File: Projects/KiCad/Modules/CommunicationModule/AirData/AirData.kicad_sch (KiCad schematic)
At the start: 30 parts, among them J1 Conn_01x08, SW1 SW_DIP_x02, U1 MCP2562-E-P, U2 MCP2515-I/P, U3 NJM7805SDL1, U4 ABX00012, Y1 8MHz

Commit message: チップ積層セラミックコンデンサをSMD1608に変更
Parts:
- C2: value 0.33μF -> 10μF; footprint Capacitor_SMD:C_0805_2012Metric_Pad1.18x1.45mm_HandSolder -> Capacitor_SMD:C_0603_1608Metric_Pad1.08x0.95mm_HandSolder
- C3, C4, C5, C6: footprint Capacitor_SMD:C_0805_2012Metric_Pad1.18x1.45mm_HandSolder -> Capacitor_SMD:C_0603_1608Metric_Pad1.08x0.95mm_HandSolder
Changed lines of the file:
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@@
       (effects (font (size 1.27 1.27)) (justify left))
     )
-    (property "Footprint" "Capacitor_SMD:C_0805_2012Metric_Pad1.18x1.45mm_HandSolder" (at 97.4852 35.56 0)
+    (property "Footprint" "Capacitor_SMD:C_0603_1608Metric_Pad1.08x0.95mm_HandSolder" (at 97.4852 35.56 0)
       (effects (font (size 1.27 1.27)) hide)
     )
@@
       (effects (font (size 1.27 1.27)) (justify left))
     )
-    (property "Footprint" "Capacitor_SMD:C_0805_2012Metric_Pad1.18x1.45mm_HandSolder" (at 150.8252 30.48 0)
+    (property "Footprint" "Capacitor_SMD:C_0603_1608Metric_Pad1.08x0.95mm_HandSolder" (at 150.8252 30.48 0)
       (effects (font (size 1.27 1.27)) hide)
     )
@@
       (effects (font (size 1.27 1.27)) (justify left))
     )
-    (property "Footprint" "Capacitor_SMD:C_0805_2012Metric_Pad1.18x1.45mm_HandSolder" (at 88.5952 35.56 0)
+    (property "Footprint" "Capacitor_SMD:C_0603_1608Metric_Pad1.08x0.95mm_HandSolder" (at 88.5952 35.56 0)
       (effects (font (size 1.27 1.27)) hide)
     )
@@
       (effects (font (size 1.27 1.27)) (justify left))
     )
-    (property "Footprint" "Capacitor_SMD:C_0805_2012Metric_Pad1.18x1.45mm_HandSolder" (at 223.2152 113.03 0)
+    (property "Footprint" "Capacitor_SMD:C_0603_1608Metric_Pad1.08x0.95mm_HandSolder" (at 223.2152 113.03 0)
       (effects (font (size 1.27 1.27)) hide)
     )
@@
       (effects (font (size 1.27 1.27)) (justify left))
     )
-    (property "Value" "0.33μF" (at 200.66 111.125 0)
-      (effects (font (size 1.27 1.27)) (justify left))
-    )
-    (property "Footprint" "Capacitor_SMD:C_0805_2012Metric_Pad1.18x1.45mm_HandSolder" (at 197.8152 113.03 0)
-      (effects (font (size 1.27 1.27)) hide)
-    )
+    (property "Value" "10μF" (at 200.66 111.125 0)
+      (effects (font (size 1.27 1.27)) (justify left))
+    )
+    (property "Footprint" "Capacitor_SMD:C_0603_1608Metric_Pad1.08x0.95mm_HandSolder" (at 197.8152 113.03 0)
+      (effects (font (size 1.27 1.27)) hide)
+    )

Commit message: 抵抗の在庫に合わせてサイズを変更
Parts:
- R3, R4, R5, R6, R7: footprint Resistor_SMD:R_0603_1608Metric_Pad0.98x0.95mm_HandSolder -> Resistor_SMD:R_0805_2012Metric_Pad1.20x1.40mm_HandSolder
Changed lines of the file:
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@@
       (effects (font (size 1.27 1.27)))
     )
-    (property "Footprint" "Resistor_SMD:R_0603_1608Metric_Pad0.98x0.95mm_HandSolder" (at 156.21 70.358 90)
+    (property "Footprint" "Resistor_SMD:R_0805_2012Metric_Pad1.20x1.40mm_HandSolder" (at 156.21 70.358 90)
       (effects (font (size 1.27 1.27)) hide)
     )
@@
       (effects (font (size 1.27 1.27)) (justify left))
     )
-    (property "Footprint" "Resistor_SMD:R_0603_1608Metric_Pad0.98x0.95mm_HandSolder" (at 61.722 166.37 90)
+    (property "Footprint" "Resistor_SMD:R_0805_2012Metric_Pad1.20x1.40mm_HandSolder" (at 61.722 166.37 90)
       (effects (font (size 1.27 1.27)) hide)
     )
@@
       (effects (font (size 1.27 1.27)) (justify left))
     )
-    (property "Footprint" "Resistor_SMD:R_0603_1608Metric_Pad0.98x0.95mm_HandSolder" (at 82.042 166.37 90)
+    (property "Footprint" "Resistor_SMD:R_0805_2012Metric_Pad1.20x1.40mm_HandSolder" (at 82.042 166.37 90)
       (effects (font (size 1.27 1.27)) hide)
     )
@@
       (effects (font (size 1.27 1.27)) (justify left))
     )
-    (property "Footprint" "Resistor_SMD:R_0603_1608Metric_Pad0.98x0.95mm_HandSolder" (at 71.882 166.37 90)
+    (property "Footprint" "Resistor_SMD:R_0805_2012Metric_Pad1.20x1.40mm_HandSolder" (at 71.882 166.37 90)
       (effects (font (size 1.27 1.27)) hide)
     )
@@
       (effects (font (size 1.27 1.27)) (justify left))
     )
-    (property "Footprint" "Resistor_SMD:R_0603_1608Metric_Pad0.98x0.95mm_HandSolder" (at 92.202 166.37 90)
-      (effects (font (size 1.27 1.27)) hide)
-    )
+    (property "Footprint" "Resistor_SMD:R_0805_2012Metric_Pad1.20x1.40mm_HandSolder" (at 92.202 166.37 90)
+      (effects (font (size 1.27 1.27)) hide)
+    )

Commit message: コネクタのピン配置を変更
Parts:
- J1: footprint Connector_Hirose:Hirose_DF11-8DP-2DSA_2x04_P2.00mm_Vertical -> Hirose_Connector:Hirose_DF11B-8DP-2DS
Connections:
- net CAN_L: now also J1.5 (Pin_5), J1.6 (Pin_6); no longer J1.3 (Pin_3), J1.4 (Pin_4)
- net GND: now also J1.3 (Pin_3), J1.4 (Pin_4); no longer J1.5 (Pin_5), J1.6 (Pin_6)
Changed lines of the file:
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@@
     (stroke (width 0) (type default))
-  )
-  (label "CAN_L" (at 43.18 35.56 180) (fields_autoplaced)
-    (effects (font (size 1.27 1.27)) (justify right bottom))
   )
   (label "CAN_H" (at 43.18 25.4 180) (fields_autoplaced)
@@
     (effects (font (size 1.27 1.27)) (justify left bottom))
   )
-  (label "GND" (at 43.18 30.48 180) (fields_autoplaced)
-    (effects (font (size 1.27 1.27)) (justify right bottom))
-  )
   (label "CAN_H" (at 43.18 53.34 180) (fields_autoplaced)
     (effects (font (size 1.27 1.27)) (justify right bottom))
@@
   )
   (label "+12V" (at 43.18 40.64 180) (fields_autoplaced)
+    (effects (font (size 1.27 1.27)) (justify right bottom))
+  )
+  (label "GND" (at 43.18 35.56 180) (fields_autoplaced)
+    (effects (font (size 1.27 1.27)) (justify right bottom))
+  )
+  (label "CAN_L" (at 43.18 30.48 180) (fields_autoplaced)
     (effects (font (size 1.27 1.27)) (justify right bottom))
   )
@@
       (effects (font (size 1.27 1.27)))
     )
-    (property "Footprint" "Connector_Hirose:Hirose_DF11-8DP-2DSA_2x04_P2.00mm_Vertical" (at 26.67 34.29 0)
-      (effects (font (size 1.27 1.27)) hide)
-    )
+    (property "Footprint" "Hirose_Connector:Hirose_DF11B-8DP-2DS" (at 26.67 34.29 0)
+      (effects (font (size 1.27 1.27)) hide)
+    )

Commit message: クリスタルをSMDに変更
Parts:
- Y1: footprint Crystal:Crystal_HC49-U_Vertical -> Crystal:Crystal_SMD_HC49-SD
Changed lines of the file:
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@@
       (effects (font (size 1.27 1.27)) (justify right))
     )
-    (property "Footprint" "Crystal:Crystal_HC49-U_Vertical" (at 257.81 33.02 0)
+    (property "Footprint" "Crystal:Crystal_SMD_HC49-SD" (at 257.81 33.02 0)
       (effects (font (size 1.27 1.27)) hide)
     )

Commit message: バッファコンデンサを表面実装に変更
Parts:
- C8: value 100μF -> 47μF; footprint Capacitor_SMD:CP_Elec_6.3x7.7 -> Capacitor_SMD:CP_Elec_6.3x5.9
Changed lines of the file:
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@@
       (effects (font (size 1.27 1.27)) (justify left))
     )
-    (property "Value" "100μF" (at 238.76 110.236 0)
+    (property "Value" "47μF" (at 238.76 110.236 0)
       (effects (font (size 1.27 1.27)) (justify left))
     )
-    (property "Footprint" "Capacitor_SMD:CP_Elec_6.3x7.7" (at 235.9152 113.03 0)
+    (property "Footprint" "Capacitor_SMD:CP_Elec_6.3x5.9" (at 235.9152 113.03 0)
       (effects (font (size 1.27 1.27)) hide)
     )

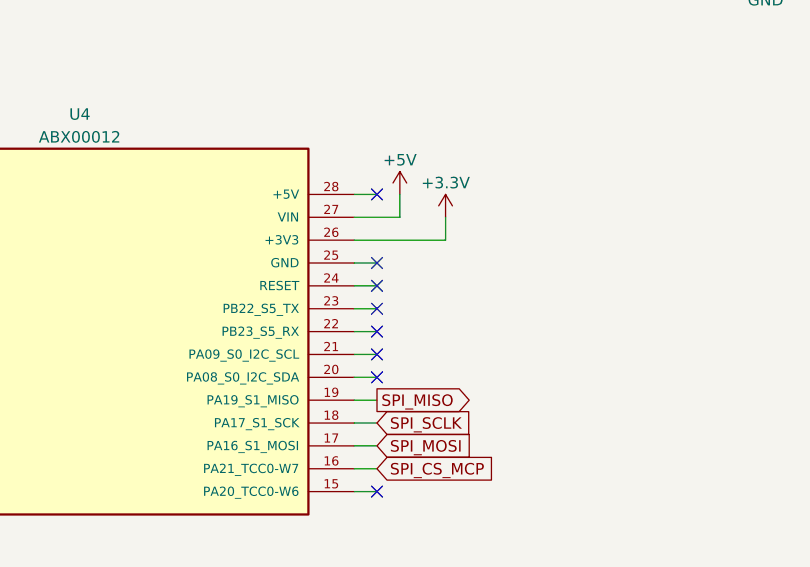
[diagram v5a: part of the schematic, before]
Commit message: 配線の繋ぎ忘れを修正
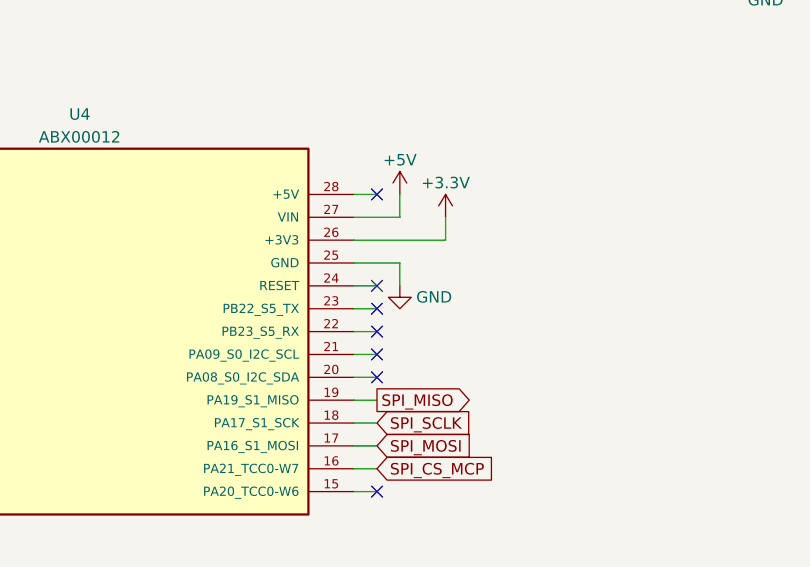
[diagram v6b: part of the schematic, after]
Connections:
- net GND: now also U4.25 (GND)
- no-connect marks 17 -> 16
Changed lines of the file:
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@@
   (no_connect (at 123.19 95.25))
   (no_connect (at 57.15 105.41))
-  (no_connect (at 123.19 102.87))
   (no_connect (at 57.15 110.49))
   (no_connect (at 57.15 95.25))
@@
     (stroke (width 0) (type default))
   )
-  (wire (pts (xy 120.65 102.87) (xy 123.19 102.87))
+  (wire (pts (xy 120.65 102.87) (xy 125.73 102.87))
     (stroke (width 0) (type default))
   )
@@
   )
   (wire (pts (xy 80.01 57.15) (xy 83.82 57.15))
+    (stroke (width 0) (type default))
+  )
+  (wire (pts (xy 125.73 102.87) (xy 125.73 105.41))
     (stroke (width 0) (type default))
   )
@@
         )
       )
+    )
+  )
+  (symbol (lib_id "power:GND") (at 125.73 105.41 0) (mirror y) (unit 1)
+    (in_bom yes) (on_board yes) (dnp no)
+    (property "Reference" "#PWR029" (at 125.73 111.76 0)
+      (effects (font (size 1.27 1.27)) hide)
+    )
+    (property "Value" "GND" (at 129.54 106.68 0)
+      (effects (font (size 1.27 1.27)))
+    )
+    (property "Footprint" "" (at 125.73 105.41 0)
+      (effects (font (size 1.27 1.27)) hide)
+    )
+    (property "Datasheet" "" (at 125.73 105.41 0)
+      (effects (font (size 1.27 1.27)) hide)
+    )
+    (pin "1")
+    (instances
+      (project "AirData"
+        (path "/ea1ed597-7cd3-4340-902e-bdce8f2d7a62"
+          (reference "#PWR029") (unit 1)
+        )
+      )

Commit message: ガーバーを再生成
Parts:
- C2: value 10μF -> 10uF
- C3, C4, C5, C6: value 0.1μF -> 0.1uF
- C8: value 47μF -> 47uF
- D2, D3, D5, D6: value ORANGE -> BLUE
- R1: value 120Ω -> 120R
- R2: value 620Ω -> 620R
- R3: value 10kΩ -> 10kR
- R4, R5, R6, R7: value 100Ω -> 100R
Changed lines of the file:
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@@
       (effects (font (size 1.27 1.27)) (justify right))
     )
-    (property "Value" "ORANGE" (at 97.79 179.3874 90)
+    (property "Value" "BLUE" (at 97.79 179.3874 90)
       (effects (font (size 1.27 1.27)) (justify right))
     )
@@
       (effects (font (size 1.27 1.27)) (justify right))
     )
-    (property "Value" "ORANGE" (at 67.31 179.3874 90)
+    (property "Value" "BLUE" (at 67.31 179.3874 90)
       (effects (font (size 1.27 1.27)) (justify right))
     )
@@
       (effects (font (size 1.27 1.27)))
     )
-    (property "Value" "10kΩ" (at 156.21 66.04 90)
+    (property "Value" "10kR" (at 156.21 66.04 90)
       (effects (font (size 1.27 1.27)))
     )
@@
       (effects (font (size 1.27 1.27)) (justify left))
     )
-    (property "Value" "0.1μF" (at 99.06 33.02 0)
+    (property "Value" "0.1uF" (at 99.06 33.02 0)
       (effects (font (size 1.27 1.27)) (justify left))
     )
@@
       (effects (font (size 1.27 1.27)) (justify left))
     )
-    (property "Value" "47μF" (at 238.76 110.236 0)
+    (property "Value" "47uF" (at 238.76 110.236 0)
       (effects (font (size 1.27 1.27)) (justify left))
     )
@@
       (effects (font (size 1.27 1.27)) (justify right))
     )
-    (property "Value" "ORANGE" (at 87.63 179.3874 90)
+    (property "Value" "BLUE" (at 87.63 179.3874 90)
       (effects (font (size 1.27 1.27)) (justify right))
     )
@@
       (effects (font (size 1.27 1.27)) (justify left))
     )
-    (property "Value" "100Ω" (at 66.04 167.6399 0)
+    (property "Value" "100R" (at 66.04 167.6399 0)
       (effects (font (size 1.27 1.27)) (justify left))
     )
@@
       (effects (font (size 1.27 1.27)) (justify left))
     )
-    (property "Value" "0.1μF" (at 152.4 27.94 0)
+    (property "Value" "0.1uF" (at 152.4 27.94 0)
       (effects (font (size 1.27 1.27)) (justify left))
     )
@@
       (effects (font (size 1.27 1.27)) (justify left))
     )
-    (property "Value" "100Ω" (at 86.36 167.6399 0)
+    (property "Value" "100R" (at 86.36 167.6399 0)
       (effects (font (size 1.27 1.27)) (justify left))
     )
@@
       (effects (font (size 1.27 1.27)) (justify left))
     )
-    (property "Value" "0.1μF" (at 90.17 33.02 0)
+    (property "Value" "0.1uF" (at 90.17 33.02 0)
       (effects (font (size 1.27 1.27)) (justify left))
     )
@@
       (effects (font (size 1.27 1.27)) (justify left))
     )
-    (property "Value" "0.1μF" (at 226.06 111.125 0)
+    (property "Value" "0.1uF" (at 226.06 111.125 0)
       (effects (font (size 1.27 1.27)) (justify left))
     )
@@
       (effects (font (size 1.27 1.27)) (justify left))
     )
-    (property "Value" "10μF" (at 200.66 111.125 0)
+    (property "Value" "10uF" (at 200.66 111.125 0)
       (effects (font (size 1.27 1.27)) (justify left))
     )
@@
       (effects (font (size 1.27 1.27)) (justify left))
     )
-    (property "Value" "620Ω" (at 57.15 167.6399 0)
+    (property "Value" "620R" (at 57.15 167.6399 0)
       (effects (font (size 1.27 1.27)) (justify left))
     )
@@
       (effects (font (size 1.27 1.27)) (justify left))
     )
-    (property "Value" "100Ω" (at 76.2 167.6399 0)
+    (property "Value" "100R" (at 76.2 167.6399 0)
       (effects (font (size 1.27 1.27)) (justify left))
     )
@@
       (effects (font (size 1.27 1.27)) (justify right))
     )
-    (property "Value" "ORANGE" (at 77.47 179.3874 90)
+    (property "Value" "BLUE" (at 77.47 179.3874 90)
       (effects (font (size 1.27 1.27)) (justify right))
     )
@@
       (effects (font (size 1.27 1.27)) (justify left))
     )
-    (property "Value" "120Ω" (at 85.09 54.61 0)
+    (property "Value" "120R" (at 85.09 54.61 0)
       (effects (font (size 1.27 1.27)) (justify left))
     )
@@
       (effects (font (size 1.27 1.27)) (justify left))
     )
-    (property "Value" "100Ω" (at 96.52 167.6399 0)
-      (effects (font (size 1.27 1.27)) (justify left))
-    )
+    (property "Value" "100R" (at 96.52 167.6399 0)
+      (effects (font (size 1.27 1.27)) (justify left))
+    )
